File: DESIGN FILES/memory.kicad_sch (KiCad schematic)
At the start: 24 parts, among them J1 TF-15x15, U2 IS25WP064A-JBLE, U3 IS42S16160J-6BLI, U4 IRLML6401

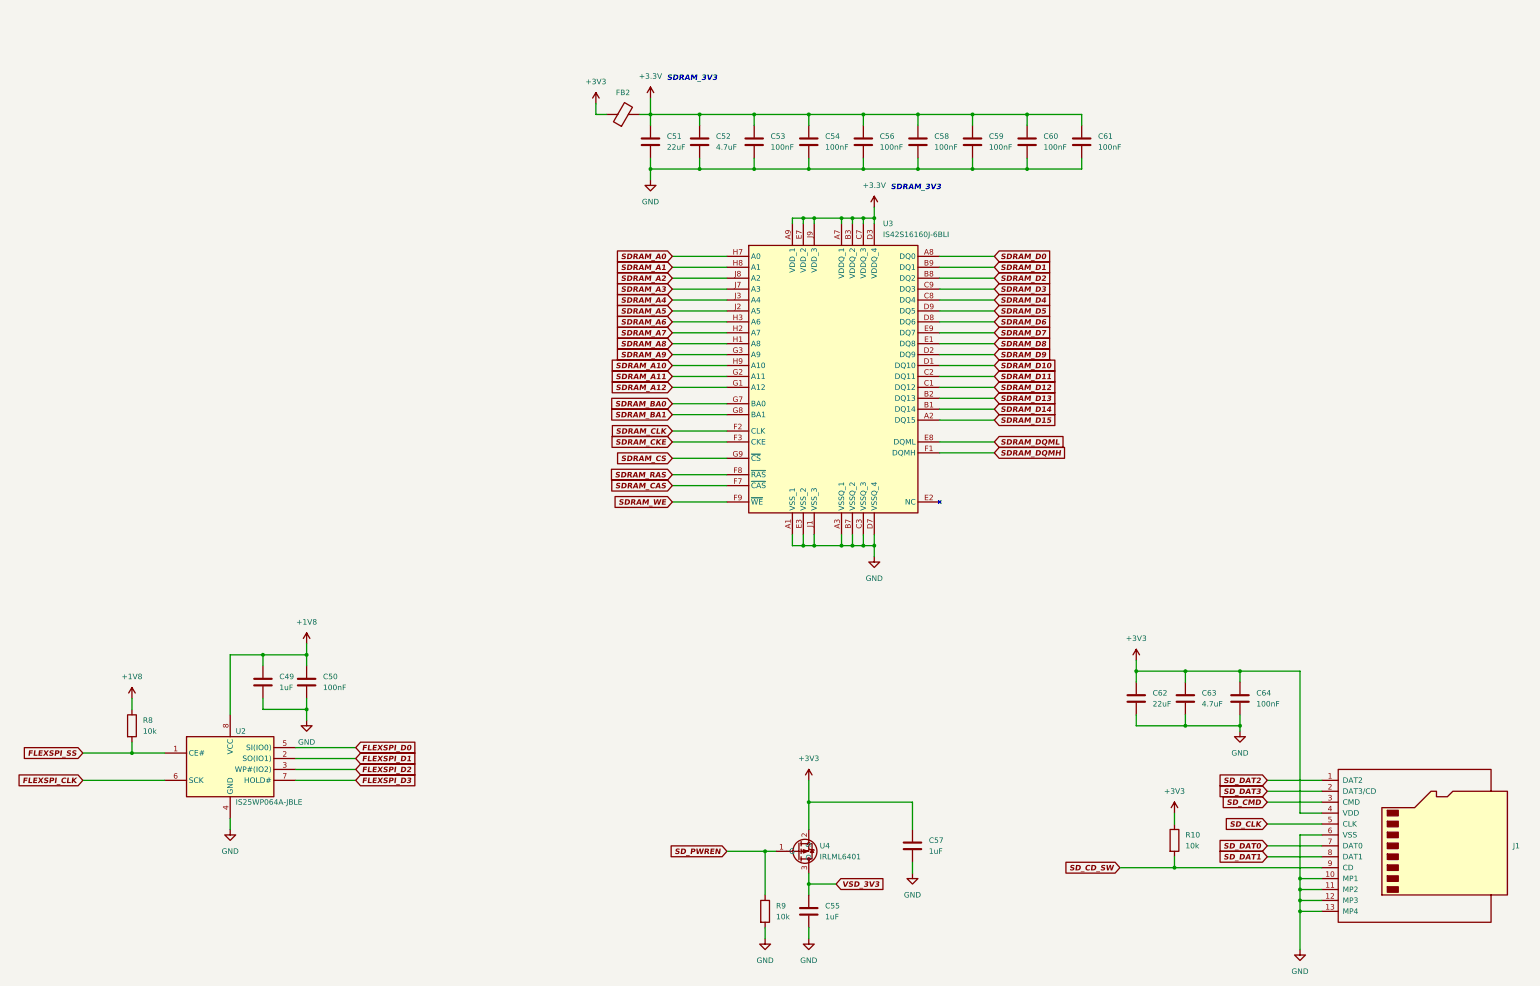
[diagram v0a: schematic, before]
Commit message: Adding voltage monitor and manual reset circuit
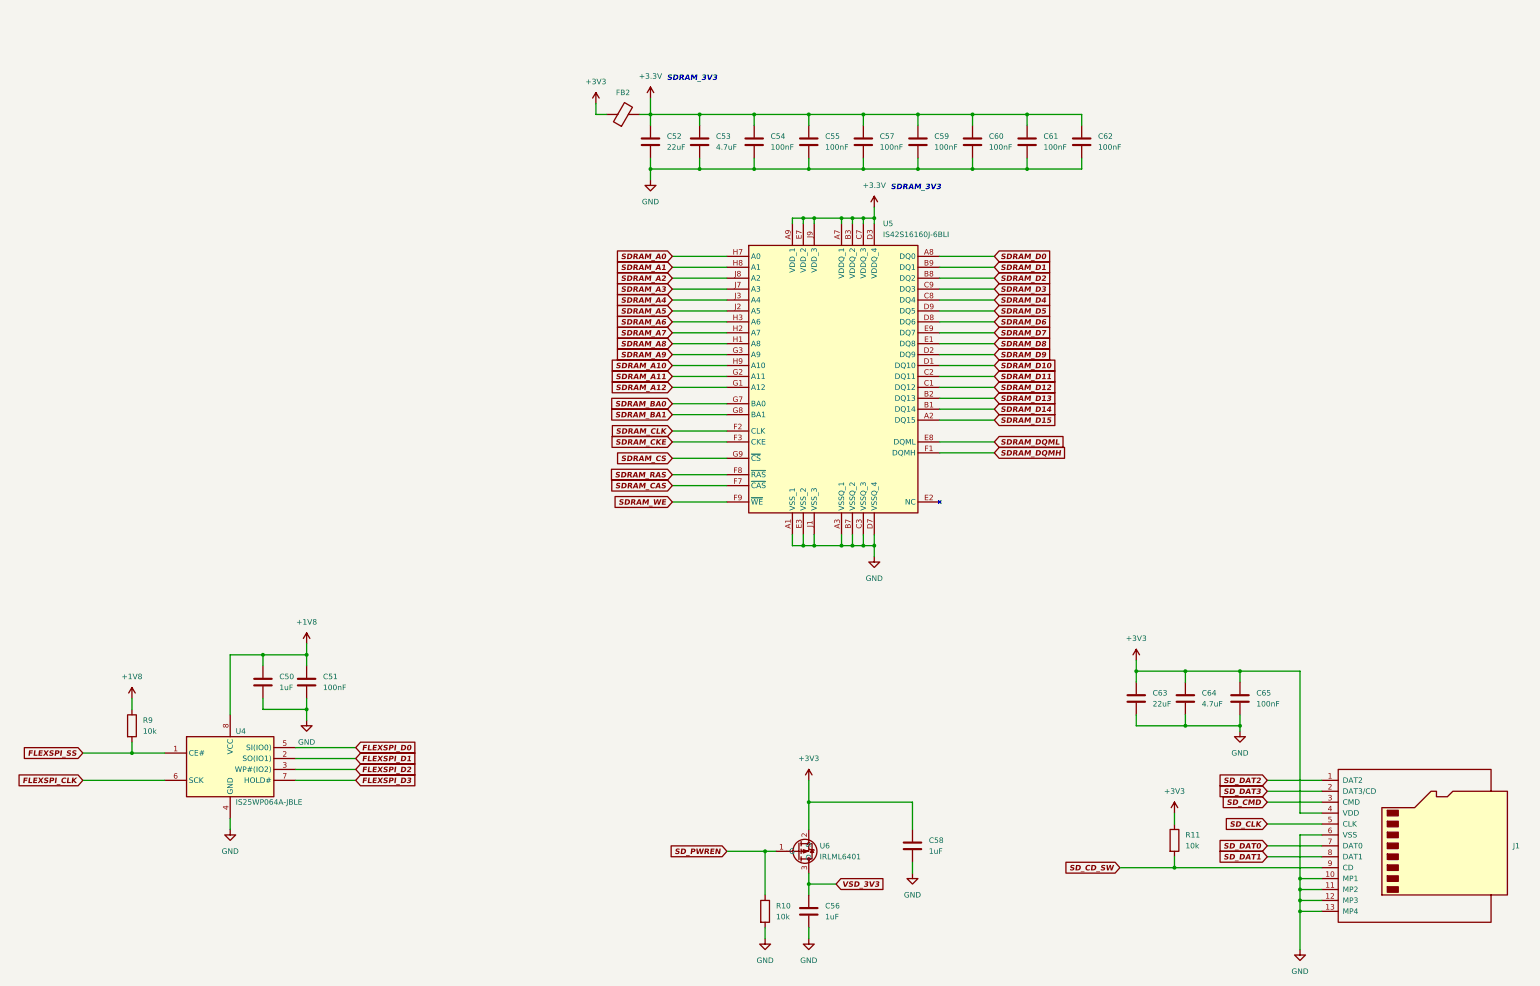
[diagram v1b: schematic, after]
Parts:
- renumbered C49 to C50, C50 to C51, C51 to C52, C52 to C53, C53 to C54, C54 to C55, C55 to C56, C56 to C57, C57 to C58, C58 to C59, C59 to C60, C60 to C61, C61 to C62, C62 to C63, C63 to C64, C64 to C65, R9 to R10, R10 to R11, R8 to R9, U2 to U4, U3 to U5, U4 to U6
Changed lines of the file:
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@@
   (symbol (lib_id "MIMXRT1064 MCU Module:CL05B104KB54PNC") (at 232.41 49.53 0) (unit 1)
     (in_bom yes) (on_board yes) (fields_autoplaced)
-    (property "Reference" "C58" (id 0) (at 236.22 48.2599 0)
+    (property "Reference" "C59" (id 0) (at 236.22 48.2599 0)
       (effects (font (size 1.27 1.27)) (justify left))
     )
@@
   (symbol (lib_id "MIMXRT1064 MCU Module:CL05B104KB54PNC") (at 90.17 175.26 0) (unit 1)
     (in_bom yes) (on_board yes) (fields_autoplaced)
-    (property "Reference" "C50" (id 0) (at 93.98 173.9899 0)
+    (property "Reference" "C51" (id 0) (at 93.98 173.9899 0)
       (effects (font (size 1.27 1.27)) (justify left))
     )
@@
   (symbol (lib_id "MIMXRT1064 MCU Module:CL05B104KB54PNC") (at 270.51 49.53 0) (unit 1)
     (in_bom yes) (on_board yes) (fields_autoplaced)
-    (property "Reference" "C61" (id 0) (at 274.32 48.2599 0)
+    (property "Reference" "C62" (id 0) (at 274.32 48.2599 0)
       (effects (font (size 1.27 1.27)) (justify left))
     )
@@
   (symbol (lib_id "MIMXRT1064 MCU Module:CL05B104KB54PNC") (at 307.34 179.07 0) (unit 1)
     (in_bom yes) (on_board yes) (fields_autoplaced)
-    (property "Reference" "C64" (id 0) (at 311.15 177.7999 0)
+    (property "Reference" "C65" (id 0) (at 311.15 177.7999 0)
       (effects (font (size 1.27 1.27)) (justify left))
     )
@@
   (symbol (lib_id "MIMXRT1064 MCU Module:CL05A105KA5NQNC") (at 80.01 175.26 0) (unit 1)
     (in_bom yes) (on_board yes) (fields_autoplaced)
-    (property "Reference" "C49" (id 0) (at 83.82 173.9899 0)
+    (property "Reference" "C50" (id 0) (at 83.82 173.9899 0)
       (effects (font (size 1.27 1.27)) (justify left))
     )
@@
   (symbol (lib_id "MIMXRT1064 MCU Module:CL05B104KB54PNC") (at 194.31 49.53 0) (unit 1)
     (in_bom yes) (on_board yes) (fields_autoplaced)
-    (property "Reference" "C53" (id 0) (at 198.12 48.2599 0)
+    (property "Reference" "C54" (id 0) (at 198.12 48.2599 0)
       (effects (font (size 1.27 1.27)) (justify left))
     )
@@
   (symbol (lib_id "MIMXRT1064 MCU Module:0402WGF1002TCE") (at 196.85 228.6 0) (unit 1)
     (in_bom yes) (on_board yes) (fields_autoplaced)
-    (property "Reference" "R9" (id 0) (at 199.39 227.3299 0)
+    (property "Reference" "R10" (id 0) (at 199.39 227.3299 0)
       (effects (font (size 1.27 1.27)) (justify left))
     )
@@
   (symbol (lib_id "MIMXRT1064 MCU Module:CL10A226MQ8NRNC") (at 170.18 49.53 0) (unit 1)
     (in_bom yes) (on_board yes) (fields_autoplaced)
-    (property "Reference" "C51" (id 0) (at 173.99 48.2599 0)
+    (property "Reference" "C52" (id 0) (at 173.99 48.2599 0)
       (effects (font (size 1.27 1.27)) (justify left))
     )
@@
   (symbol (lib_id "MIMXRT1064 MCU Module:CL05B104KB54PNC") (at 207.01 49.53 0) (unit 1)
     (in_bom yes) (on_board yes) (fields_autoplaced)
-    (property "Reference" "C54" (id 0) (at 210.82 48.2599 0)
+    (property "Reference" "C55" (id 0) (at 210.82 48.2599 0)
       (effects (font (size 1.27 1.27)) (justify left))
     )
@@
   (symbol (lib_id "MIMXRT1064 MCU Module:CL05B104KB54PNC") (at 219.71 49.53 0) (unit 1)
     (in_bom yes) (on_board yes) (fields_autoplaced)
-    (property "Reference" "C56" (id 0) (at 223.52 48.2599 0)
+    (property "Reference" "C57" (id 0) (at 223.52 48.2599 0)
       (effects (font (size 1.27 1.27)) (justify left))
     )
@@
   (symbol (lib_id "MIMXRT1064 MCU Module:0402WGF1002TCE") (at 49.53 185.42 0) (unit 1)
     (in_bom yes) (on_board yes) (fields_autoplaced)
-    (property "Reference" "R8" (id 0) (at 52.07 184.1499 0)
+    (property "Reference" "R9" (id 0) (at 52.07 184.1499 0)
       (effects (font (size 1.27 1.27)) (justify left))
     )
@@
   (symbol (lib_id "MIMXRT1064 MCU Module:CL05A105KA5NQNC") (at 207.01 228.6 0) (unit 1)
     (in_bom yes) (on_board yes) (fields_autoplaced)
-    (property "Reference" "C55" (id 0) (at 210.82 227.3299 0)
+    (property "Reference" "C56" (id 0) (at 210.82 227.3299 0)
       (effects (font (size 1.27 1.27)) (justify left))
     )
@@
   (symbol (lib_id "MIMXRT1064 MCU Module:IS25WP064A-JBLE") (at 59.69 190.5 0) (unit 1)
     (in_bom yes) (on_board yes)
-    (property "Reference" "U2" (id 0) (at 73.66 186.69 0)
+    (property "Reference" "U4" (id 0) (at 73.66 186.69 0)
       (effects (font (size 1.27 1.27)) (justify left))
     )
@@
   (symbol (lib_id "MIMXRT1064 MCU Module:CL05B104KB54PNC") (at 245.11 49.53 0) (unit 1)
     (in_bom yes) (on_board yes) (fields_autoplaced)
-    (property "Reference" "C59" (id 0) (at 248.92 48.2599 0)
+    (property "Reference" "C60" (id 0) (at 248.92 48.2599 0)
       (effects (font (size 1.27 1.27)) (justify left))
     )
@@
   (symbol (lib_id "IRLML6401:IRLML6401") (at 207.01 214.63 0) (mirror x) (unit 1)
     (in_bom yes) (on_board yes)
-    (property "Reference" "U4" (id 0) (at 209.55 213.36 0)
+    (property "Reference" "U6" (id 0) (at 209.55 213.36 0)
       (effects (font (size 1.27 1.27)) (justify left))
     )
@@
   (symbol (lib_id "MIMXRT1064 MCU Module:CL10A226MQ8NRNC") (at 283.21 179.07 0) (unit 1)
     (in_bom yes) (on_board yes) (fields_autoplaced)
-    (property "Reference" "C62" (id 0) (at 287.02 177.7999 0)
+    (property "Reference" "C63" (id 0) (at 287.02 177.7999 0)
       (effects (font (size 1.27 1.27)) (justify left))
     )
@@
   (symbol (lib_id "MIMXRT1064 MCU Module:0402WGF1002TCE") (at 292.1 212.09 0) (unit 1)
     (in_bom yes) (on_board yes) (fields_autoplaced)
-    (property "Reference" "R10" (id 0) (at 294.64 210.8199 0)
+    (property "Reference" "R11" (id 0) (at 294.64 210.8199 0)
       (effects (font (size 1.27 1.27)) (justify left))
     )
@@
   (symbol (lib_id "MIMXRT1064 MCU Module:CL05A475MP5NRNC") (at 294.64 179.07 0) (unit 1)
     (in_bom yes) (on_board yes) (fields_autoplaced)
-    (property "Reference" "C63" (id 0) (at 298.45 177.7999 0)
+    (property "Reference" "C64" (id 0) (at 298.45 177.7999 0)
       (effects (font (size 1.27 1.27)) (justify left))
     )
@@
   (symbol (lib_id "MIMXRT1064 MCU Module:CL05A475MP5NRNC") (at 181.61 49.53 0) (unit 1)
     (in_bom yes) (on_board yes) (fields_autoplaced)
-    (property "Reference" "C52" (id 0) (at 185.42 48.2599 0)
+    (property "Reference" "C53" (id 0) (at 185.42 48.2599 0)
       (effects (font (size 1.27 1.27)) (justify left))
     )
@@
   (symbol (lib_id "MIMXRT1064 MCU Module:CL05B104KB54PNC") (at 257.81 49.53 0) (unit 1)
     (in_bom yes) (on_board yes) (fields_autoplaced)
-    (property "Reference" "C60" (id 0) (at 261.62 48.2599 0)
+    (property "Reference" "C61" (id 0) (at 261.62 48.2599 0)
       (effects (font (size 1.27 1.27)) (justify left))
     )
@@
   (symbol (lib_id "MIMXRT1064 MCU Module:IS42S16160J-6BLI") (at 187.96 76.2 0) (unit 1)
     (in_bom yes) (on_board yes) (fields_autoplaced)
-    (property "Reference" "U3" (id 0) (at 224.2694 68.58 0)
+    (property "Reference" "U5" (id 0) (at 224.2694 68.58 0)
       (effects (font (size 1.27 1.27)) (justify left))
     )
@@
   (symbol (lib_id "MIMXRT1064 MCU Module:CL05A105KA5NQNC") (at 231.14 213.36 0) (unit 1)
     (in_bom yes) (on_board yes) (fields_autoplaced)
-    (property "Reference" "C57" (id 0) (at 234.95 212.0899 0)
-      (effects (font (size 1.27 1.27)) (justify left))
-    )
+    (property "Reference" "C58" (id 0) (at 234.95 212.0899 0)
+      (effects (font (size 1.27 1.27)) (justify left))
+    )

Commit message: Refactoring schematic
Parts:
- renumbered C50 to C41, C51 to C42, C52 to C43, C53 to C44, C54 to C45, C55 to C46, C56 to C47, C57 to C48, C58 to C49, C59 to C50, C60 to C51, C61 to C52, C62 to C53, C63 to C54, C64 to C55, C65 to C56, R9 to R3, R10 to R4, R11 to R5, U4 to U2, U5 to U3, U6 to U4
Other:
- note added: "QSPI FLASH"
- note added: "SDRAM"
- note added: "uSD CARD"
- note added: "uSD CARD POWER ENABLE"
- moved on the sheet: C41, C42, C43, C44, C45, C46, C47, C48, C49, C50, C51, C52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

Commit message: vcc check
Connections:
- net +3V3: no longer C54.1, C55.1, C56.1, J1.4 (VDD)
- net VSD_3V3: now also C54.1, C55.1, C56.1, J1.4 (VDD)
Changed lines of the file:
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@@
     (stroke (width 0) (type default) (color 0 0 0 0))
   )
-  (wire (pts (xy 280.67 27.94) (xy 280.67 30.48))
+  (wire (pts (xy 280.67 25.4) (xy 280.67 30.48))
     (stroke (width 0) (type default) (color 0 0 0 0))
   )
@@
     (property "Intersheet References" "${INTERSHEET_REFS}" (id 0) (at 300.3081 55.753 0)
       (effects (font (size 1.27 1.27) (thickness 0.254) bold italic) (justify right) hide)
+    )
+  )
+  (global_label "VSD_3V3" (shape input) (at 280.67 25.4 0) (fields_autoplaced)
+    (effects (font (size 1.27 1.27) bold italic) (justify left))
+    (property "Intersheet References" "${INTERSHEET_REFS}" (id 0) (at 291.5724 25.273 0)
+      (effects (font (size 1.27 1.27) bold italic) (justify left) hide)
     )
   )
@@
     (pin "2")
   )
-  (symbol (lib_id "power:+3V3") (at 280.67 27.94 0) (unit 1)
-    (in_bom yes) (on_board yes) (fields_autoplaced)
-    (property "Reference" "#PWR044" (id 0) (at 280.67 31.75 0)
-      (effects (font (size 1.27 1.27)) hide)
-    )
-    (property "Value" "+3V3" (id 1) (at 280.67 22.86 0))
-    (property "Footprint" "" (id 2) (at 280.67 27.94 0)
-      (effects (font (size 1.27 1.27)) hide)
-    )
-    (property "Datasheet" "" (id 3) (at 280.67 27.94 0)
-      (effects (font (size 1.27 1.27)) hide)
-    )
-    (pin "1")
-  )
   (symbol (lib_id "power:+3V3") (at 289.56 63.5 0) (unit 1)

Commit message: schematic and lib edit
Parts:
- removed U4: IRLML6401, MIMXRT1064 MCU Module:IRLML6401, symbol IRLML6401:IRLML6401
- added Q1: IRLML6401, MIMXRT1064 MCU Module:IRLML6401, symbol MIMXRT1064 MCU Module:IRLML6401
- renumbered C43 to C41, C44 to C42, C45 to C43, C46 to C44, C41 to C45, C48 to C46, C42 to C47, C50 to C48, C51 to C49, C52 to C50, C53 to C51, C47 to C52, C49 to C53, U3 to U2, U2 to U3
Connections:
- net +3V3: now also Q1.3 (D)
- net SD_PWREN: now also Q1.1 (G)
- net VSD_3V3: now also Q1.2 (S)
